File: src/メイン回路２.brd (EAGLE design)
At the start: 6 parts

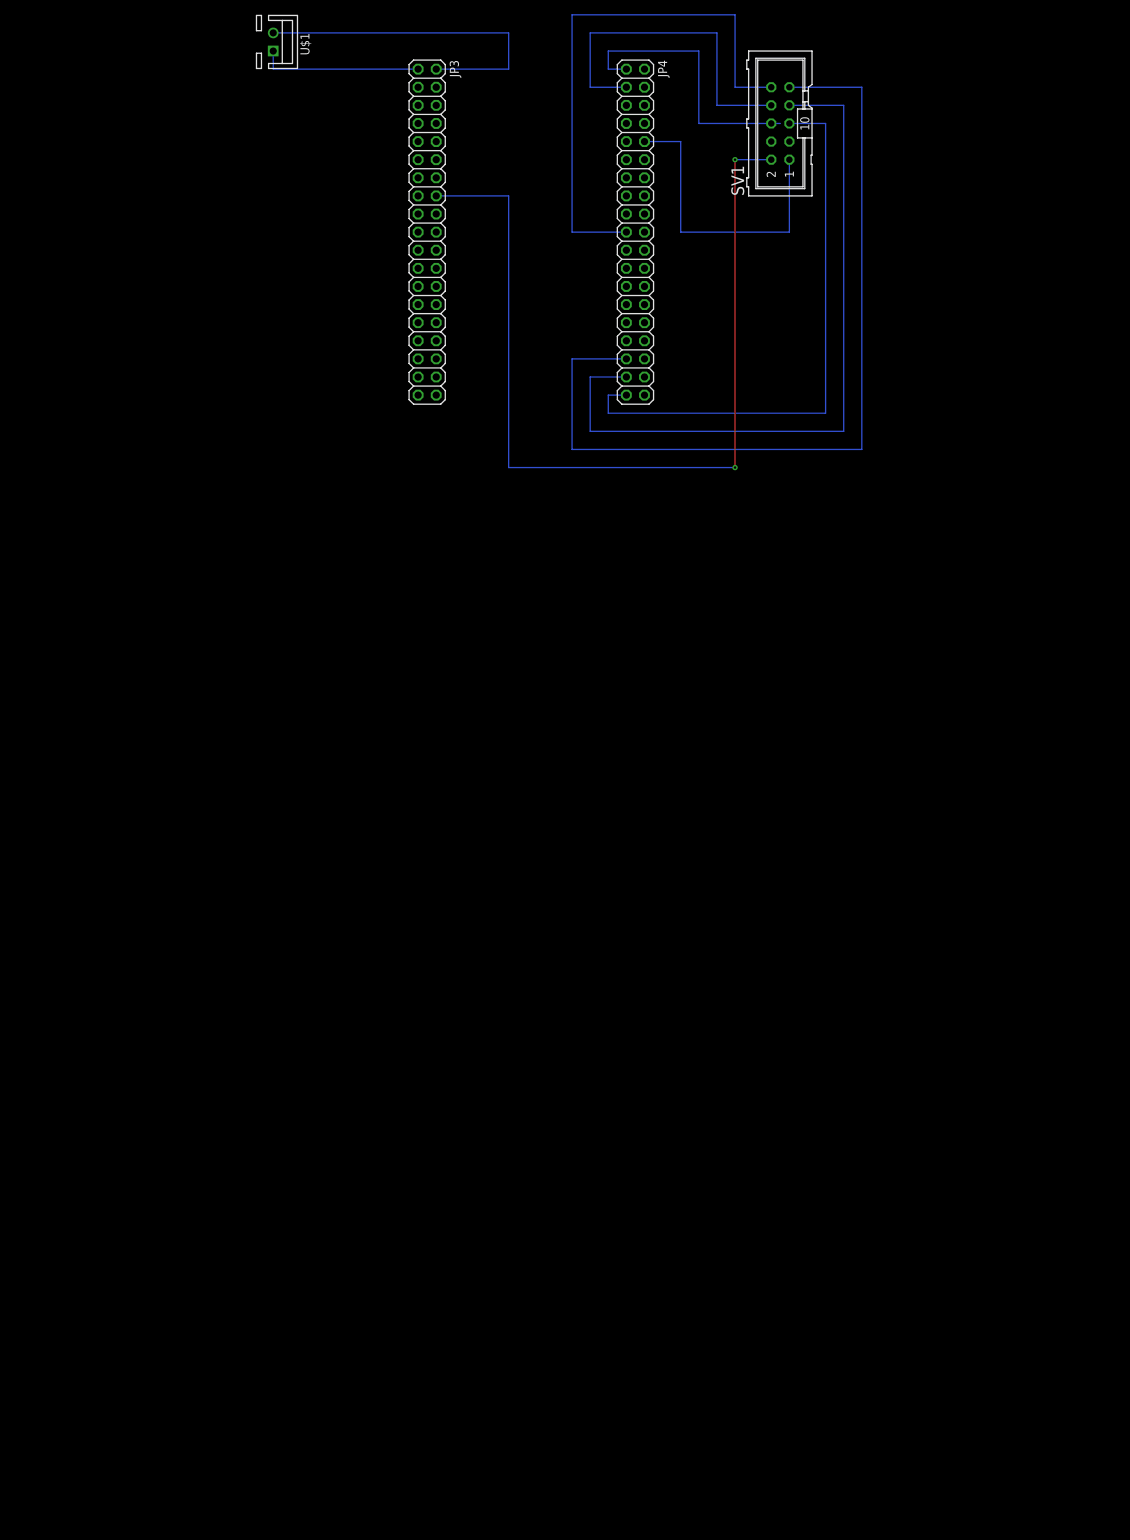
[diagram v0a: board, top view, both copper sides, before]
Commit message: [fix]受信側の回路のsch修正全て
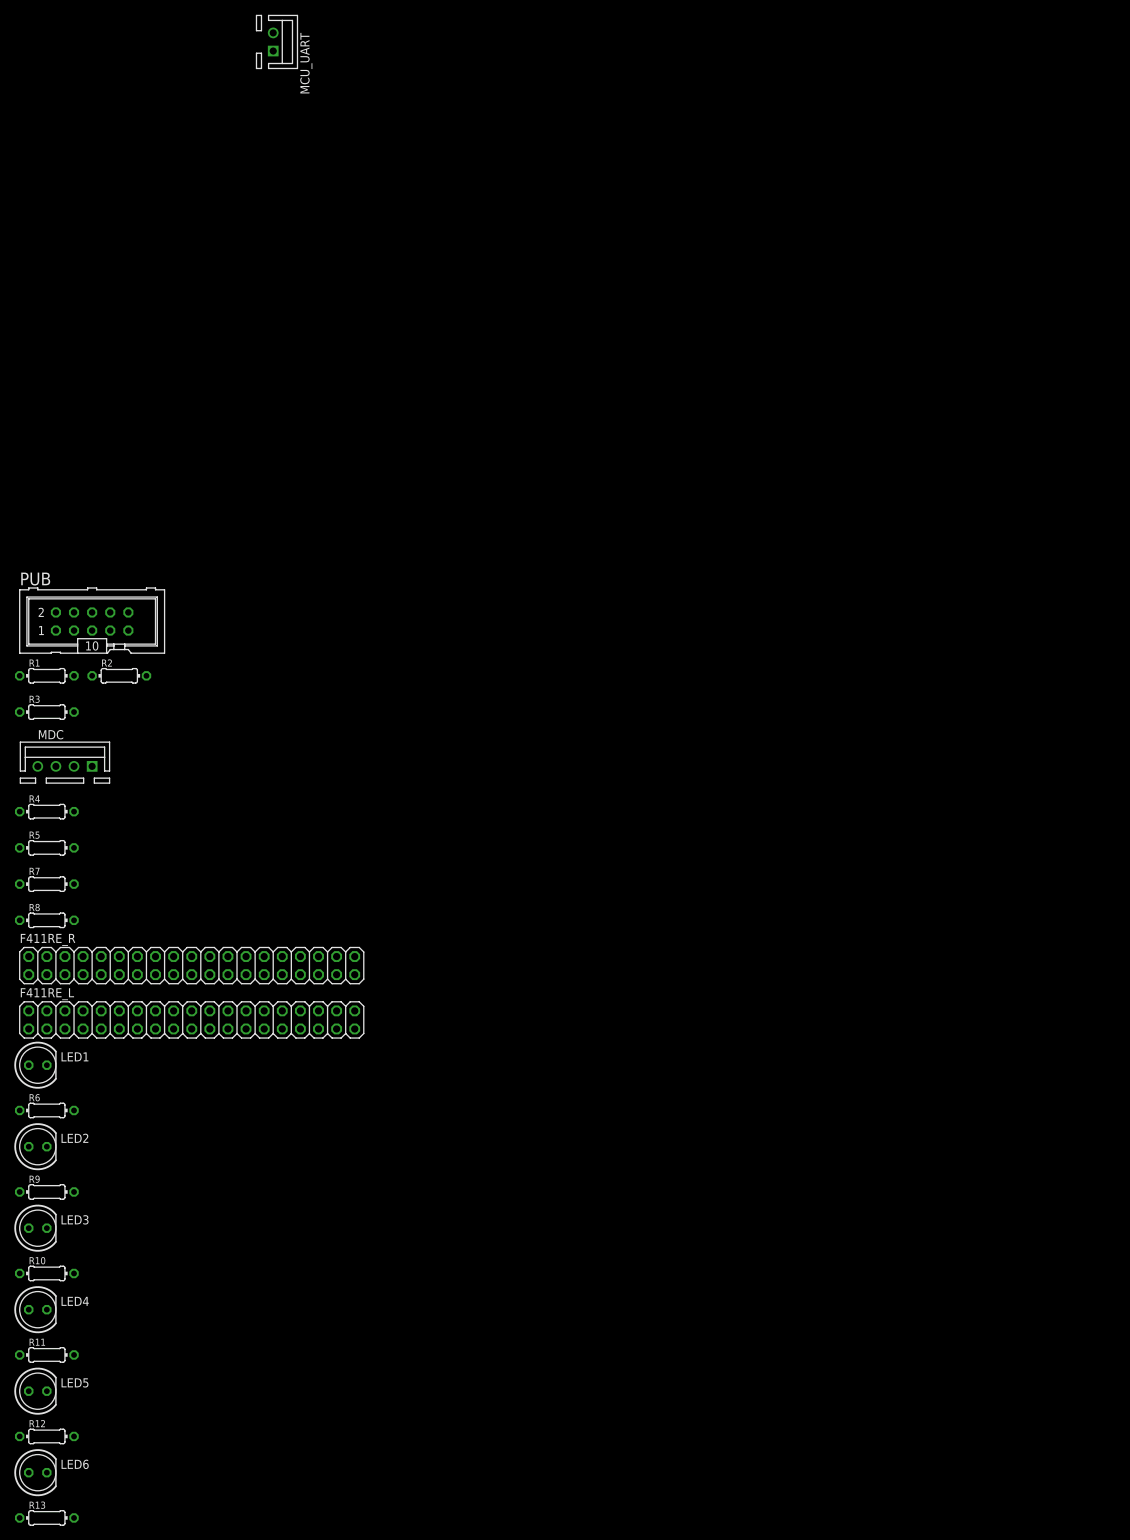
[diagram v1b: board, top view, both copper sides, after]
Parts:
- removed JP3, JP4: (no value), pinhead:2X19
- removed SV1: (no value), con-ml:ML10
- added F411RE_L, F411RE_R: (no value), pinhead:2X19
- added LED1, LED2, LED3, LED4, LED5, LED6: (no value), led:LED5MM
- added MDC: (no value), con-jst-xh:B4B-XH
- added PUB: (no value), con-ml:ML10
- added R1, R2, R3: 330, rcl:0204/7
- added R10, R11, R12, R13, R6, R9: 100, rcl:0204/7
- added R4, R5, R7: 2.2k, rcl:0204/7
- added R8: 3.3k, rcl:0204/7
- renumbered U$1 to MCU_UART
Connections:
- removed net N$10: JP4.10, SV1.1
- removed net N$11: JP3.16, SV1.2
- removed net N$12: JP3.2, MCU_UART.2
- removed net N$13: JP3.1, MCU_UART.1
- removed net N$7: JP4.35, SV1.7
- removed net N$8: JP4.33, SV1.9
- new net 3V: PUB.2, R7.1, R8.2
- new net DIR1: F411RE_R.27, PUB.9
- new net DIR2: F411RE_R.25, PUB.7
- new net DIR3: F411RE_R.23, PUB.5
- new net GND: F411RE_L.20, F411RE_L.22, F411RE_R.20, LED1.K, LED2.K, LED3.K, LED4.K, LED5.K, LED6.K, MDC.4, PUB.1, R1.1, R2.1, R3.1, R8.1
- new net LED1: F411RE_R.11, R6.1
- new net LED2: F411RE_R.19, R9.1
- new net LED3: F411RE_R.21, R10.1
- new net LED4: F411RE_R.17, R11.1
- new net LED5: F411RE_R.15, R12.1
- new net LED6: F411RE_R.13, R13.1
- new net N$1: LED2.A, R9.2
- new net N$5: LED5.A, R12.2
- new net PWM1: F411RE_R.29, PUB.10, R1.2
- new net PWM2: F411RE_R.31, PUB.8, R2.2
- new net PWM3: F411RE_R.33, PUB.6, R3.2
- new net RX_MCU: F411RE_L.21, MCU_UART.1
- new net SCL: F411RE_R.3, MDC.3, R5.1
- new net SDA: F411RE_R.5, MDC.2, R4.1
- new net TX_MCU: F411RE_L.17, MCU_UART.2
- new net U5V: F411RE_R.8, MDC.1, R4.2, R5.2, R7.2
- net N$2: now also LED1.A, R6.2; no longer JP4.1, SV1.6
- net N$3: now also LED3.A, R10.2; no longer JP4.3, SV1.8
- net N$4: now also LED4.A, R11.2; no longer JP4.19, SV1.10
- net N$6: now also LED6.A, R13.2; no longer JP4.37, SV1.5
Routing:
- net N$11: track 128.3 -> 0.00 mm, vias 2 -> 0
- net N$8: track 121.9 -> 0.00 mm
- net N$7: track 101.6 -> 0.00 mm
- net N$6: track 81.3 -> 0.00 mm
- net N$4: track 76.2 -> 0.00 mm
- net N$3: track 48.3 -> 0.00 mm
- net N$12: track 48.3 -> 0.00 mm
- net N$10: track 43.2 -> 0.00 mm
- net N$2: track 39.4 -> 0.00 mm
- net N$13: track 22.9 -> 0.00 mm

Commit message: [fix]brd途中まで変更
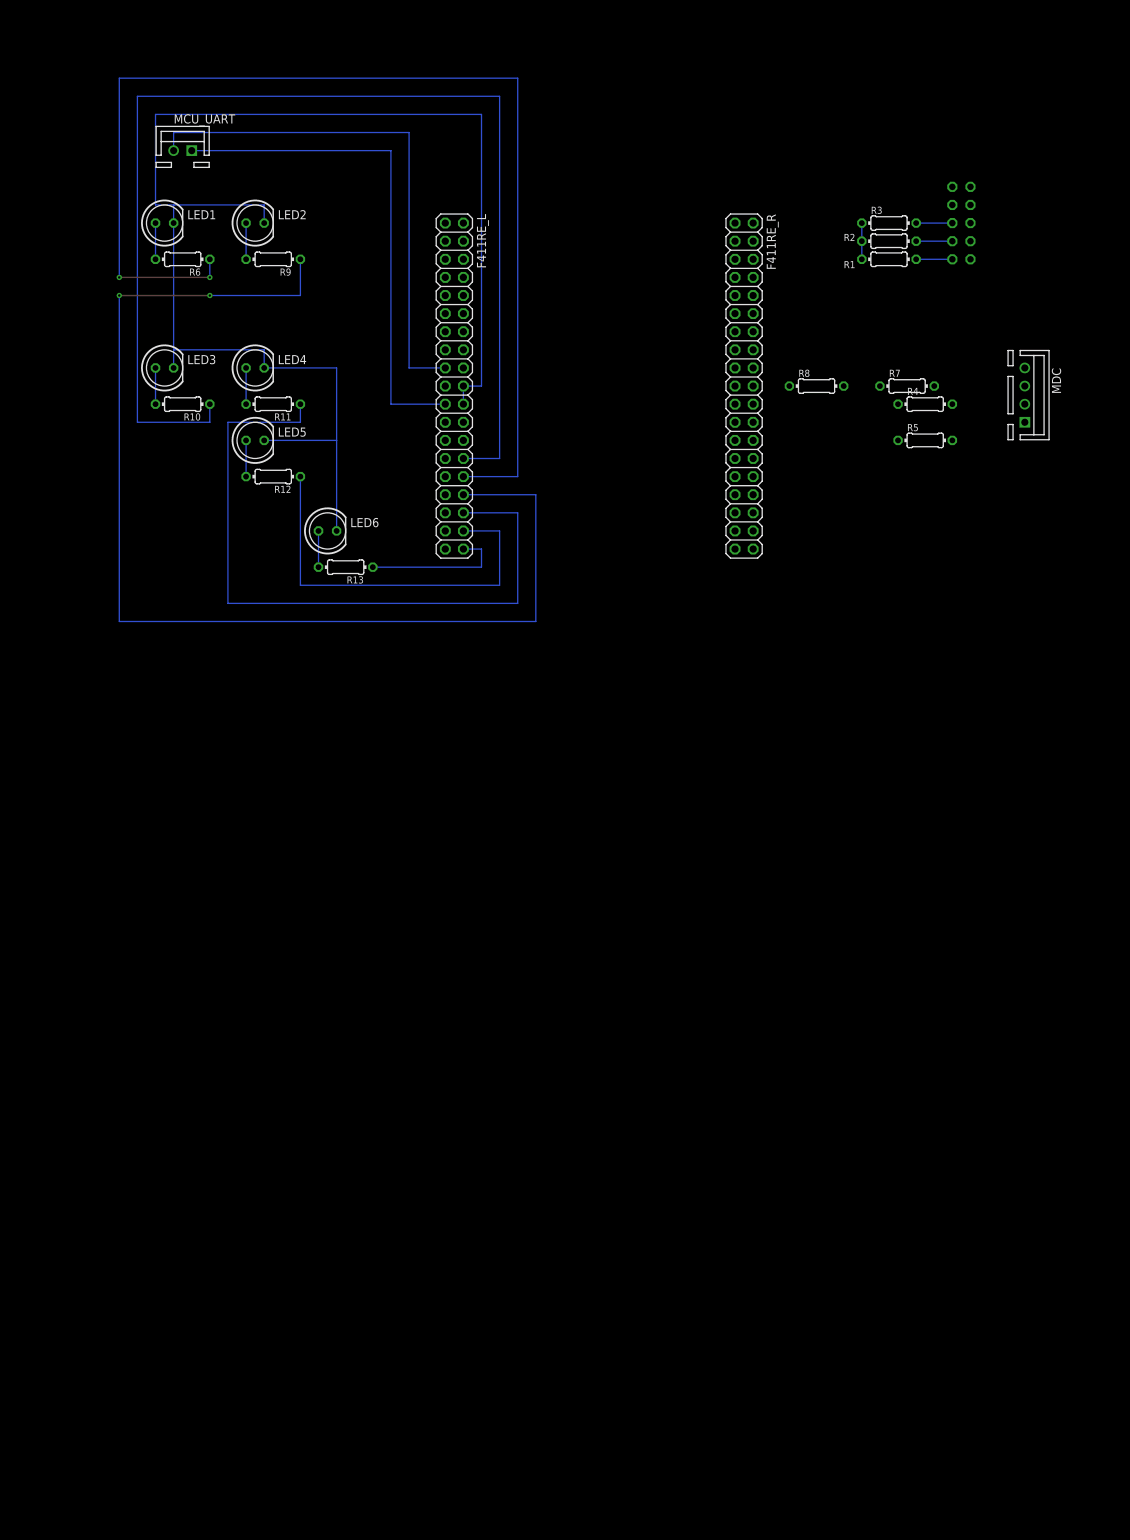
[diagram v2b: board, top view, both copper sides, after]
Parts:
- moved MDC 144.3 mm to (124.5, 25.4), turned to 270 degrees
- moved R13 139.8 mm to (29.2, 1.27), turned to 180 degrees
- moved R7 139.4 mm to (108.0, 26.7)
- moved R12 138.3 mm to (19.1, 14.0), turned to 180 degrees
- moved LED6 138.2 mm to (26.7, 6.35)
- moved R11 137.1 mm to (19.1, 24.1), turned to 180 degrees
- moved LED5 136.8 mm to (16.5, 19.1)
- moved R3 136.6 mm to (105.4, 49.5)
- moved R4 135.8 mm to (110.5, 24.1)
- moved R5 135.8 mm to (110.5, 19.1)
- moved LED4 135.6 mm to (16.5, 29.2)
- moved R9 134.6 mm to (19.1, 44.5), turned to 180 degrees
- moved PUB 134.1 mm to (115.6, 49.5), flipped to the bottom, turned to 270 degrees
- moved LED2 133.1 mm to (16.5, 49.5)
- moved R1 131.8 mm to (105.4, 44.5)
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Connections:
- net LED1: now also F411RE_L.30; no longer F411RE_R.11
- net LED2: now also F411RE_L.32; no longer F411RE_R.19
- net LED3: now also F411RE_L.28; no longer F411RE_R.21
- net LED4: now also F411RE_L.34; no longer F411RE_R.17
- net LED5: now also F411RE_L.36; no longer F411RE_R.15
- net LED6: now also F411RE_L.38; no longer F411RE_R.13
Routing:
- net GND: track 0.00 -> 205.7 mm
- net LED3: track 0.00 -> 165.1 mm
- net LED2: track 0.00 -> 162.6 mm, vias 0 -> 2
- net LED1: track 0.00 -> 162.6 mm, vias 0 -> 2
- net LED4: track 0.00 -> 99.1 mm
- net TX_MCU: track 0.00 -> 73.7 mm
- net RX_MCU: track 0.00 -> 71.1 mm
- net LED5: track 0.00 -> 55.9 mm
- net LED6: track 0.00 -> 20.3 mm
- net N$4: track 0.00 -> 5.08 mm
- net N$3: track 0.00 -> 5.08 mm
- net N$6: track 0.00 -> 5.08 mm
- net N$5: track 0.00 -> 5.08 mm
- net PWM3: track 0.00 -> 5.08 mm
- net PWM2: track 0.00 -> 5.08 mm
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
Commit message: [complete]メイン回路2の完成
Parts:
- moved R8 45.2 mm to (123.2, 62.2), turned to 180 degrees
- moved R7 35.9 mm to (113.0, 62.2), turned to 180 degrees
- moved R1 9.67 mm to (114.3, 48.3), turned to 270 degrees
- moved R5 7.41 mm to (116.8, 15.2), turned to 90 degrees
- moved R2 7.41 mm to (111.8, 50.8), turned to 270 degrees
- moved R4 6.48 mm to (116.8, 25.4), turned to 270 degrees
- moved F411RE_L 6.35 mm to (38.1, 26.7)
- moved R3 5.39 mm to (109.2, 53.3), turned to 270 degrees
- moved PUB 5.08 mm to (120.7, 49.5)
- moved F411RE_R 5.08 mm to (90.2, 26.7)
- moved MDC 3.59 mm to (121.9, 22.9), flipped to the bottom, turned to 90 degrees
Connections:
- net GND: now also PUB.3, PUB.4
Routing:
- net SDA: track 0.00 -> 205.7 mm
- net DIR3: track 0.00 -> 167.6 mm
- net DIR2: track 0.00 -> 147.3 mm
- net GND: track 205.7 -> 336.1 mm, vias 0 -> 2
- net SCL: track 0.00 -> 128.1 mm
- net DIR1: track 0.00 -> 127.0 mm
- net PWM1: track 5.08 -> 111.8 mm
- net PWM2: track 5.08 -> 101.6 mm
- net U5V: track 0.00 -> 91.4 mm, vias 0 -> 2
- net PWM3: track 5.08 -> 91.4 mm
- net 3V: track 0.00 -> 10.2 mm
- net RX_MCU: track 71.1 -> 64.8 mm
- net TX_MCU: track 73.7 -> 67.3 mm
- net LED2: track 162.6 -> 158.7 mm
- net LED4: track 99.1 -> 95.2 mm
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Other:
- board outline added: 3.8 x 15.2 mm
- board text added: "上"
- board text added: "下"
- board text added: "受信確認(MCU)"
- board text added: "受信確認(MDC)"
- board text added: "発射!!!!!!"
- board text added: "装填機構"
- board text added: "速度確認(PWM)"

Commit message: [complete]メイン回路1の完成
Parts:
- moved R3 17.8 mm to (127.0, 53.3)
- moved R2 12.7 mm to (124.5, 50.8)
- moved R1 7.62 mm to (121.9, 48.3)
- moved PUB 5.08 mm to (115.6, 49.5), flipped to the top
- moved R7 2.54 mm to (110.5, 62.2)
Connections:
- net DIR1: now also F411RE_R.29; no longer F411RE_R.27
- net DIR2: now also F411RE_R.31; no longer F411RE_R.25
- net DIR3: now also F411RE_R.33; no longer F411RE_R.23
- net PWM1: now also F411RE_R.27; no longer F411RE_R.29
- net PWM2: now also F411RE_R.25; no longer F411RE_R.31
- net PWM3: now also F411RE_R.23; no longer F411RE_R.33
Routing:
- net PWM3: track 91.4 -> 172.7 mm
- net DIR3: track 167.6 -> 86.4 mm
- net PWM2: track 101.6 -> 152.4 mm
- net DIR2: track 147.3 -> 96.5 mm
- net SDA: track 205.7 -> 231.1 mm
- net DIR1: track 127.0 -> 106.7 mm
- net PWM1: track 111.8 -> 132.1 mm
- net SCL: track 128.1 -> 138.2 mm
- net GND: track 336.1 -> 343.7 mm
- net 3V: track 10.2 -> 15.2 mm, vias 0 -> 1
- net U5V: track 91.4 -> 88.9 mm
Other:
- board text added: "はんだ付けの順番に注意!!"
